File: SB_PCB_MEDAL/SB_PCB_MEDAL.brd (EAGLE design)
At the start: 60 x 60 mm, 41 parts, among them IC1 ATTINY44A-SSU

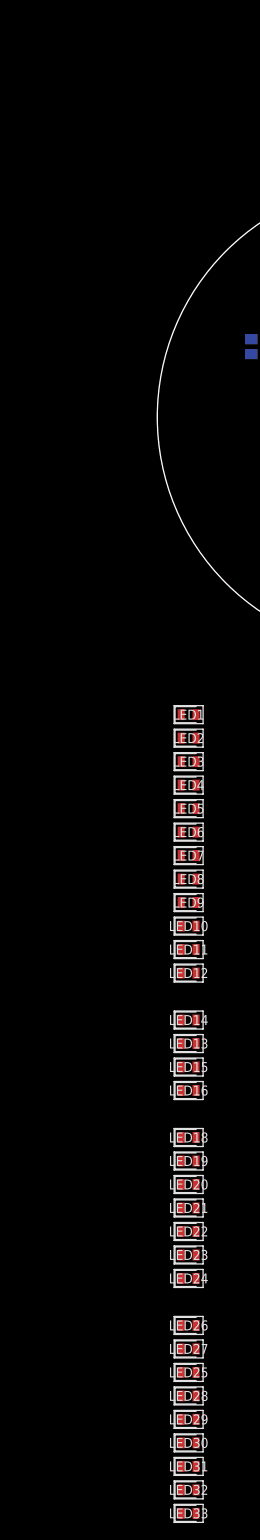
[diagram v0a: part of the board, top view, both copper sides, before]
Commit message: removed 2 additional LEDs
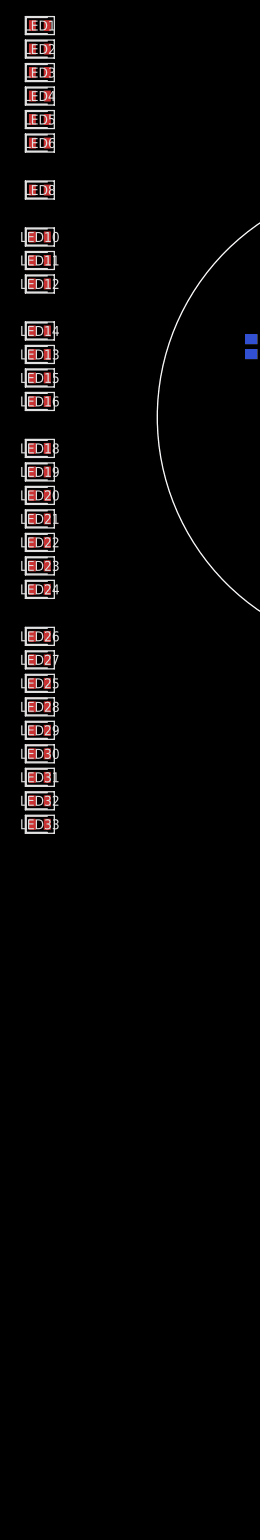
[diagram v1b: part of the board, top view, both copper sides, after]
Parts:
- removed LED7, LED9: KPT-2012CGCK, SamacSys_Parts:LEDC2012X78N
- moved LED1 90.0 mm to (-45.0, 50.0)
- moved LED10 90.0 mm to (-45.0, 23.0)
- moved LED11 90.0 mm to (-45.0, 20.0)
- moved LED12 90.0 mm to (-45.0, 17.0)
- moved LED13 90.0 mm to (-45.0, 8.00)
- moved LED14 90.0 mm to (-45.0, 11.0)
- moved LED15 90.0 mm to (-45.0, 5.00)
- moved LED16 90.0 mm to (-45.0, 2.00)
- moved LED18 90.0 mm to (-45.0, -4.00)
- moved LED19 90.0 mm to (-45.0, -7.00)
- moved LED2 90.0 mm to (-45.0, 47.0)
- moved LED20 90.0 mm to (-45.0, -10.0)
- moved LED21 90.0 mm to (-45.0, -13.0)
- moved LED22 90.0 mm to (-45.0, -16.0)
- moved LED23 90.0 mm to (-45.0, -19.0)
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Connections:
- removed net N$1: LED26.2
- net N$2: no longer LED7.2
- net N$4: no longer LED7.1, LED9.2
- net N$5: no longer LED9.1

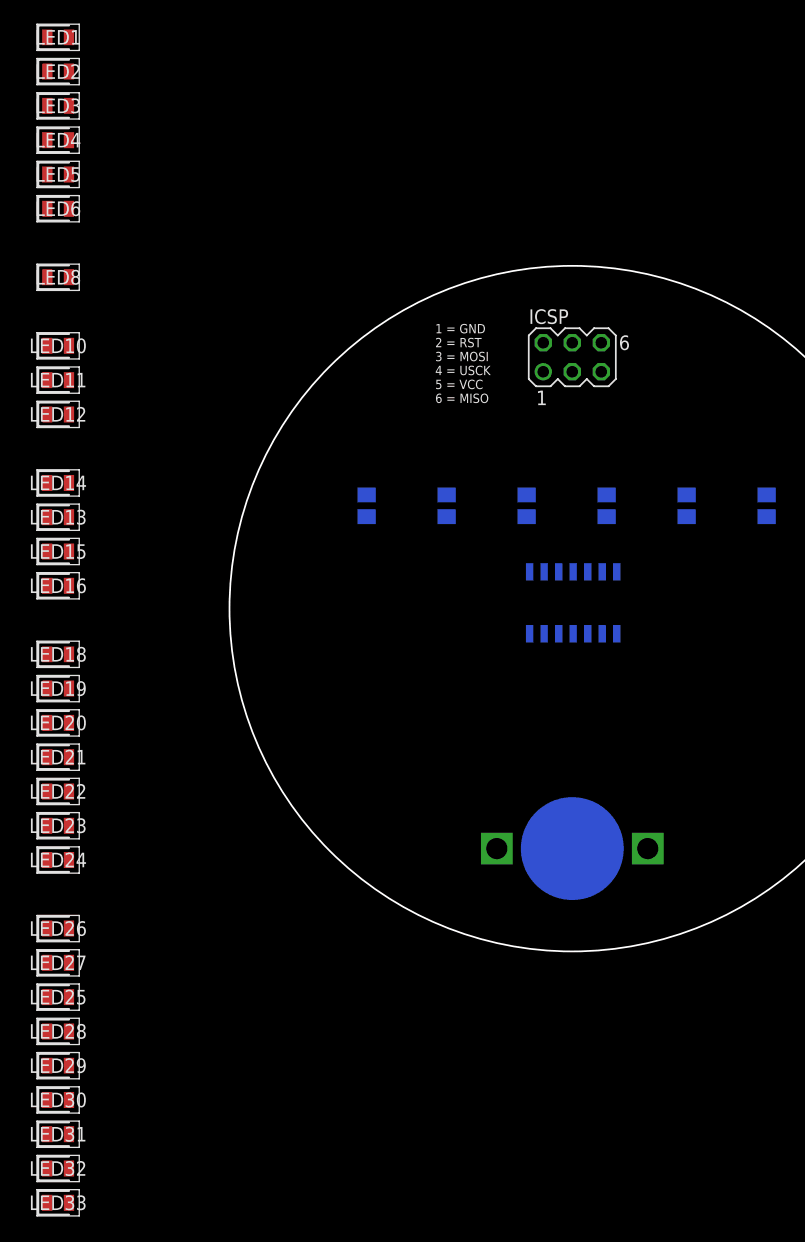
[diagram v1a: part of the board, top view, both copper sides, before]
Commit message: literally copy and paste files from other branch into the master because EAGLE files and branches hate each other as much as North Korea and the US....
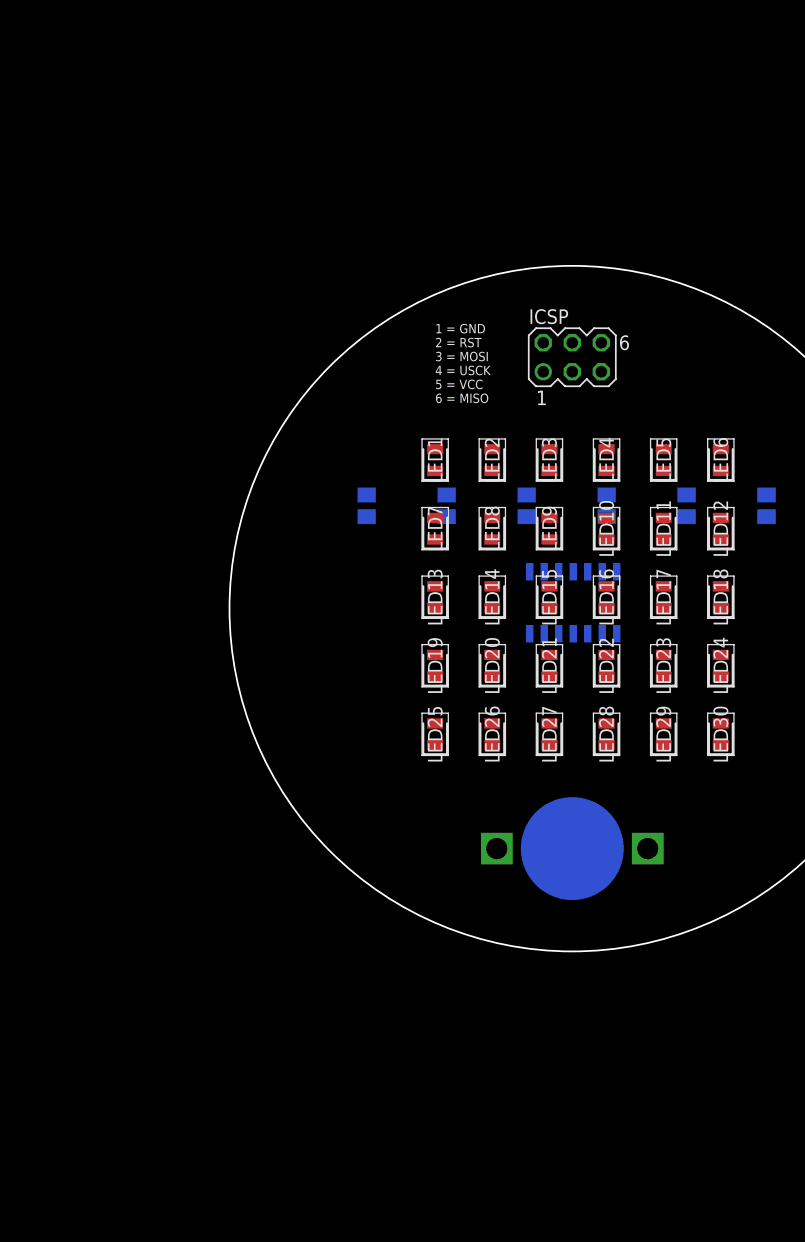
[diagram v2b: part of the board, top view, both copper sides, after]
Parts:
- removed LED31, LED32, LED33: KPT-2012CGCK, SamacSys_Parts:LEDC2012X78N
- added LED17, LED7, LED9: KPT-2012CGCK, SamacSys_Parts:LEDC2012X78N
- moved LED30 66.2 mm to (13.0, -11.0), turned to 90 degrees
- moved LED6 62.0 mm to (13.0, 13.0), turned to 90 degrees
- moved LED24 60.4 mm to (13.0, -5.00), turned to 90 degrees
- moved LED29 60.4 mm to (8.00, -11.0), turned to 90 degrees
- moved LED12 58.9 mm to (13.0, 7.00), turned to 90 degrees
- moved LED5 58.6 mm to (8.00, 13.0), turned to 90 degrees
- moved LED18 58.2 mm to (13.0, 1.00), turned to 90 degrees
- moved LED4 55.6 mm to (3.00, 13.0), turned to 90 degrees
- moved LED23 54.8 mm to (8.00, -5.00), turned to 90 degrees
- moved LED28 54.6 mm to (3.00, -11.0), turned to 90 degrees
- moved LED11 54.6 mm to (8.00, 7.00), turned to 90 degrees
- moved LED3 53.0 mm to (-2.00, 13.0), turned to 90 degrees
- moved LED2 51.0 mm to (-7.00, 13.0), turned to 90 degrees
- moved LED10 50.6 mm to (3.00, 7.00), turned to 90 degrees
- moved LED1 49.6 mm to (-12.0, 13.0), turned to 90 degrees
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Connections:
- removed net N$10: LED2.2, LED4.1
- removed net N$7: LED10.1, LED6.2
- removed net N$8: LED4.2, LED6.1
- new net N$1: LED1.2, LED11.2, LED12.1, LED19.2, LED2.1, LED20.1, LED25.2, LED26.1, LED29.2, LED30.1, R1.2
- new net N$19: IC1.5
- new net N$20: IC1.6
- new net PA0: IC1.13, R1.1
- new net PA1: IC1.12, R2.1
- new net PA2: IC1.11, R3.1
- new net PA3: IC1.10, R4.1
- new net PB0: IC1.2, R5.1
- new net PB1: IC1.3, R6.1
- net N$2: now also LED1.1, LED13.2, LED14.1, LED2.2, LED21.2, LED22.1, LED27.2, LED28.1, LED3.2, LED4.1, R2.2; no longer LED3.1, LED5.2
- net N$3: now also LED11.1, LED12.2, LED15.2, LED16.1, LED23.2, LED24.1, LED3.1, LED4.2, LED5.2, LED6.1, R3.2; no longer LED1.1, LED3.2
- net N$4: now also LED13.1, LED14.2, LED17.2, LED18.1, LED19.1, LED20.2, LED6.2, LED7.2, LED8.1, R4.2; no longer LED8.2
- net N$5: now also LED10.1, LED15.1, LED16.2, LED21.1, LED22.2, LED25.1, LED26.2, LED7.1, LED8.2, LED9.2, R5.2; no longer LED11.2, LED8.1
- net N$6: now also LED17.1, LED18.2, LED23.1, LED24.2, LED27.1, LED28.2, LED29.1, LED30.2, LED9.1, R6.2; no longer LED12.1

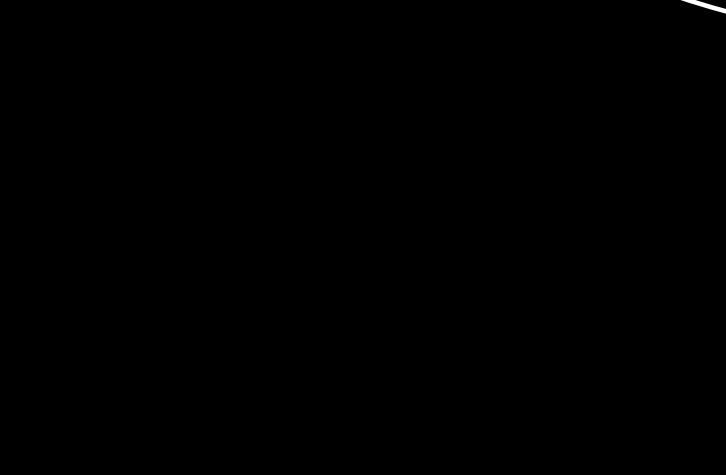
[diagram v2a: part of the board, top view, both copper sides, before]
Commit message: added surface mountable button
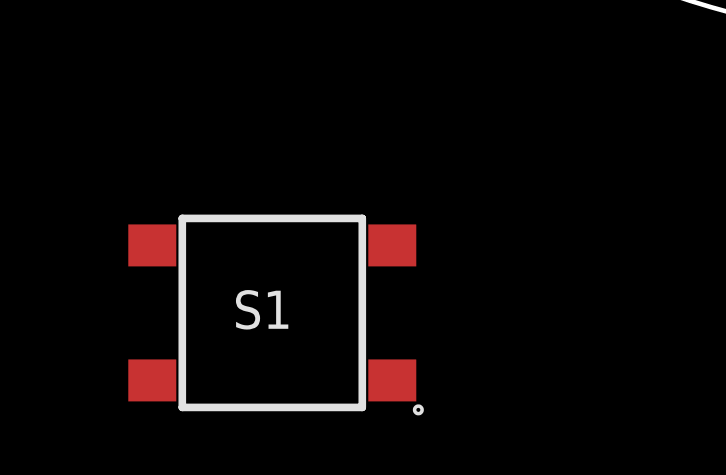
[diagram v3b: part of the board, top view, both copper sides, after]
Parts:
- added S1: B3FS-1000P, SamacSys_Parts:B3FS-1000P
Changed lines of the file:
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@@
 <attribute name="SUPPLIER_NAME" value="RS" x="13" y="-11" size="1.778" layer="27" rot="R90" display="off"/>
+</element>
+<element name="S1" library="SamacSys_Parts" package="B3FS-1000P" value="B3FS-1000P" x="-23" y="-39">
+<attribute name="3D_PACKAGE" value="" x="-23" y="-39" size="1.778" layer="27" display="off"/>
+<attribute name="ALLIED_NUMBER" value="70175891" x="-23" y="-39" size="1.778" layer="27" display="off"/>
+<attribute name="DESCRIPTION" value="Switch Tact,6x6mm,flat act,gen purp,tape Plunger Tactile Switch, SPST-NO 0.05 A@ 24 V dc 0.5mm" x="-23" y="-39" size="1.778" layer="27" display="off"/>
+<attribute name="HEIGHT" value="mm" x="-23" y="-39" size="1.778" layer="27" display="off"/>
+<attribute name="MANUFACTURER_NAME" value="Omron Electronics" x="-23" y="-39" size="1.778" layer="27" display="off"/>
+<attribute name="MANUFACTURER_PART_NUMBER" value="B3FS-1000P" x="-23" y="-39" size="1.778" layer="27" display="off"/>
+<attribute name="OTHER_PART_NUMBER" value="" x="-23" y="-39" size="1.778" layer="27" display="off"/>
+<attribute name="RS_PART_NUMBER" value="6821254P" x="-23" y="-39" size="1.778" layer="27" display="off"/>
+<attribute name="SUPPLIER_NAME" value="RS" x="-23" y="-39" size="1.778" layer="27" display="off"/>
 </element>
 </elements>

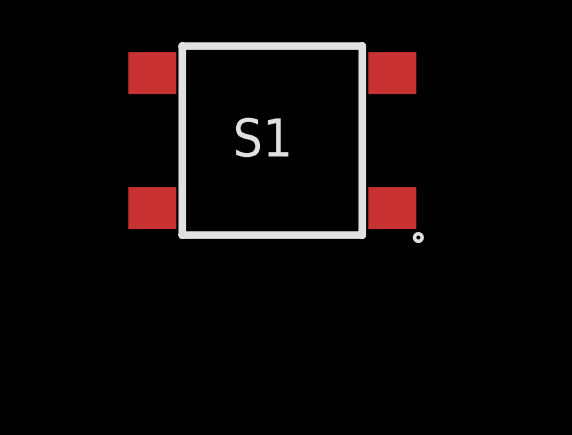
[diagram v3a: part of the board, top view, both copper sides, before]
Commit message: added more labels to the board
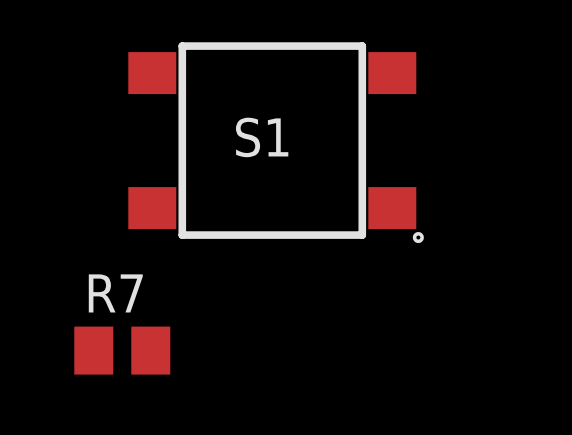
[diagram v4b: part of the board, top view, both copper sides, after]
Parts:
- added R7: 10k Ω, resistor:M0805
- BT1: value (none) -> 3v
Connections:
- removed net N$19: IC1.5
- removed net N$20: IC1.6
- new net N$7: R7.1, S1.4
- new net N$8: S1.3
- net GND: now also IC1.5, IC1.6, S1.1, S1.2
- net VCC: now also R7.2
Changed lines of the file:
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@@
 <attribute name="OC_NEWARK" value="unknown" x="0" y="22" size="1.778" layer="27" display="off"/>
 </element>
-<element name="BT1" library="SparkFun-Batteries" package="BATTCON_12MM_PTH" value="" x="0" y="-21" rot="MR0">
+<element name="BT1" library="SparkFun-Batteries" package="BATTCON_12MM_PTH" value="3v" x="0" y="-21" rot="MR0">
 <attribute name="PROD_ID" value="BATT-08315" x="0" y="-21" size="0.4064" layer="28" rot="MR0" display="off"/>
 <attribute name="SF_SKU" value="PRT-07948" x="0" y="-21" size="0.4064" layer="28" rot="MR0" display="off"/>
@@
 <attribute name="SUPPLIER_NAME" value="RS" x="-23" y="-39" size="1.778" layer="27" display="off"/>
 </element>
+<element name="R7" library="resistor" package="M0805" value="10k Ω" x="-28" y="-46"/>
 </elements>
 <signals>
@@
 <contactref element="ICSP" pad="5"/>
 <contactref element="BT1" pad="VCC@1"/>
+<contactref element="R7" pad="2"/>
+<wire x1="-6.604" y1="-21" x2="-27.05" y2="-46" width="0" layer="19" extent="1-1"/>
 <wire x1="-3.73" y1="3.221" x2="-6.604" y2="-21" width="0" layer="19" extent="16-16"/>
 <wire x1="2.54" y1="20.73" x2="-3.73" y2="3.221" width="0" layer="19" extent="16-16"/>
@@
 <contactref element="IC1" pad="14"/>
 <contactref element="BT1" pad="GND"/>
-<wire x1="-3.73" y1="-2.201" x2="0" y2="-21" width="0" layer="19" extent="1-16"/>
-<wire x1="-2.54" y1="20.73" x2="-3.73" y2="-2.201" width="0" layer="19" extent="16-16"/>
+<contactref element="IC1" pad="5"/>
+<contactref element="IC1" pad="6"/>
+<contactref element="S1" pad="2"/>
+<contactref element="S1" pad="1"/>
+<wire x1="-19" y1="-41.25" x2="-27" y2="-41.25" width="0" layer="19" extent="1-1"/>
+<wire x1="0" y1="-21" x2="-19" y2="-41.25" width="0" layer="19" extent="1-16"/>
+<wire x1="-3.73" y1="-2.201" x2="0" y2="-21" width="0" layer="19" extent="16-16"/>
+<wire x1="1.35" y1="3.221" x2="-3.73" y2="-2.201" width="0" layer="19" extent="16-16"/>
+<wire x1="2.62" y1="3.221" x2="1.35" y2="3.221" width="0" layer="19" extent="16-16"/>
+<wire x1="-2.54" y1="20.73" x2="1.35" y2="3.221" width="0" layer="19" extent="16-16"/>
 </signal>
 <signal name="MISO">
@@
 <wire x1="-1.19" y1="3.221" x2="17" y2="8.05" width="0" layer="19" extent="16-16"/>
 </signal>
-<signal name="N$19">
-<contactref element="IC1" pad="5"/>
-</signal>
-<signal name="N$20">
-<contactref element="IC1" pad="6"/>
+<signal name="N$7">
+<contactref element="S1" pad="4"/>
+<contactref element="R7" pad="1"/>
+<wire x1="-27" y1="-36.75" x2="-28.95" y2="-46" width="0" layer="19" extent="1-1"/>
+</signal>
+<signal name="N$8">
+<contactref element="S1" pad="3"/>
 </signal>
 </signals>

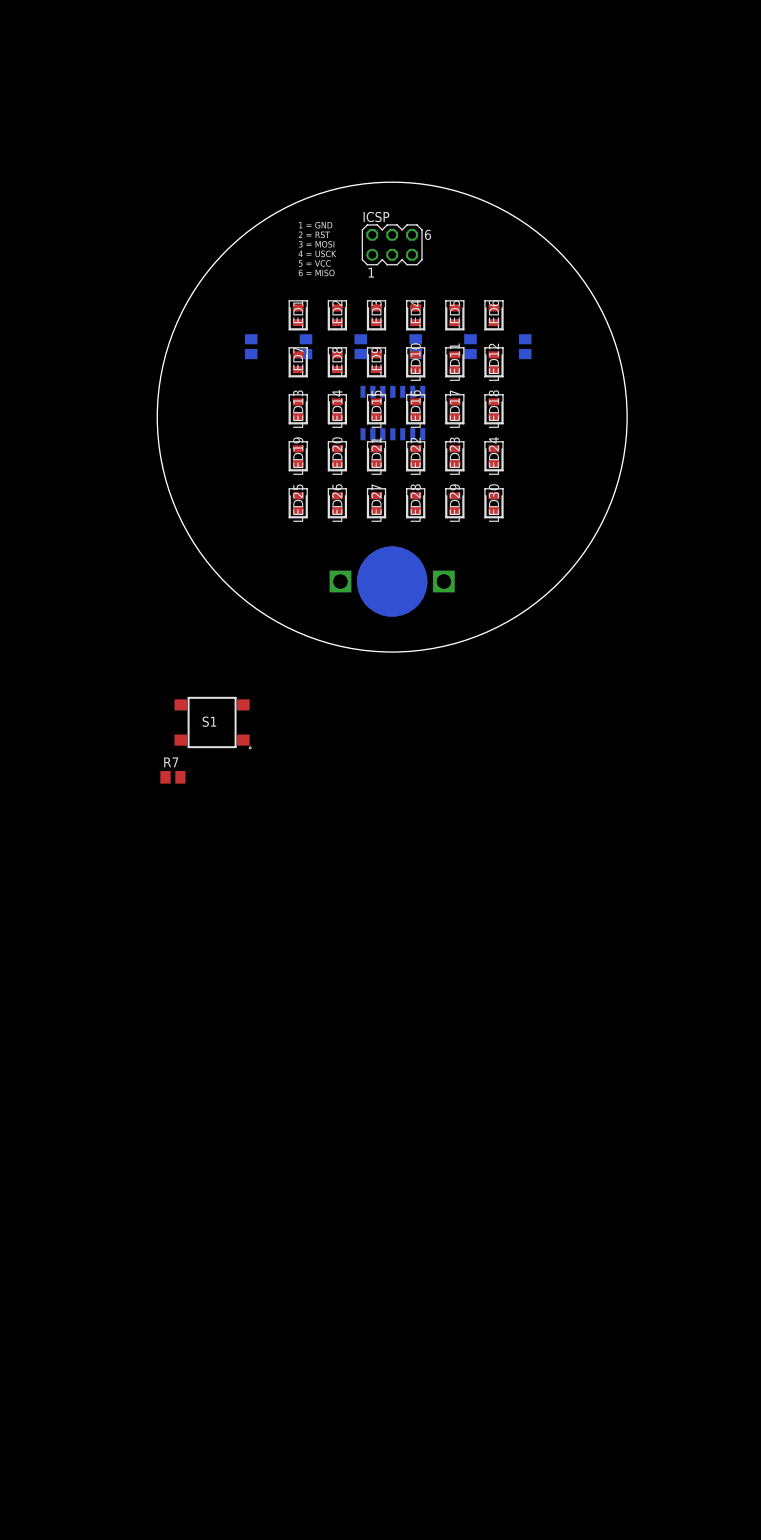
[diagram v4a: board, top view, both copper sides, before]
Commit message: modify led position and add usb
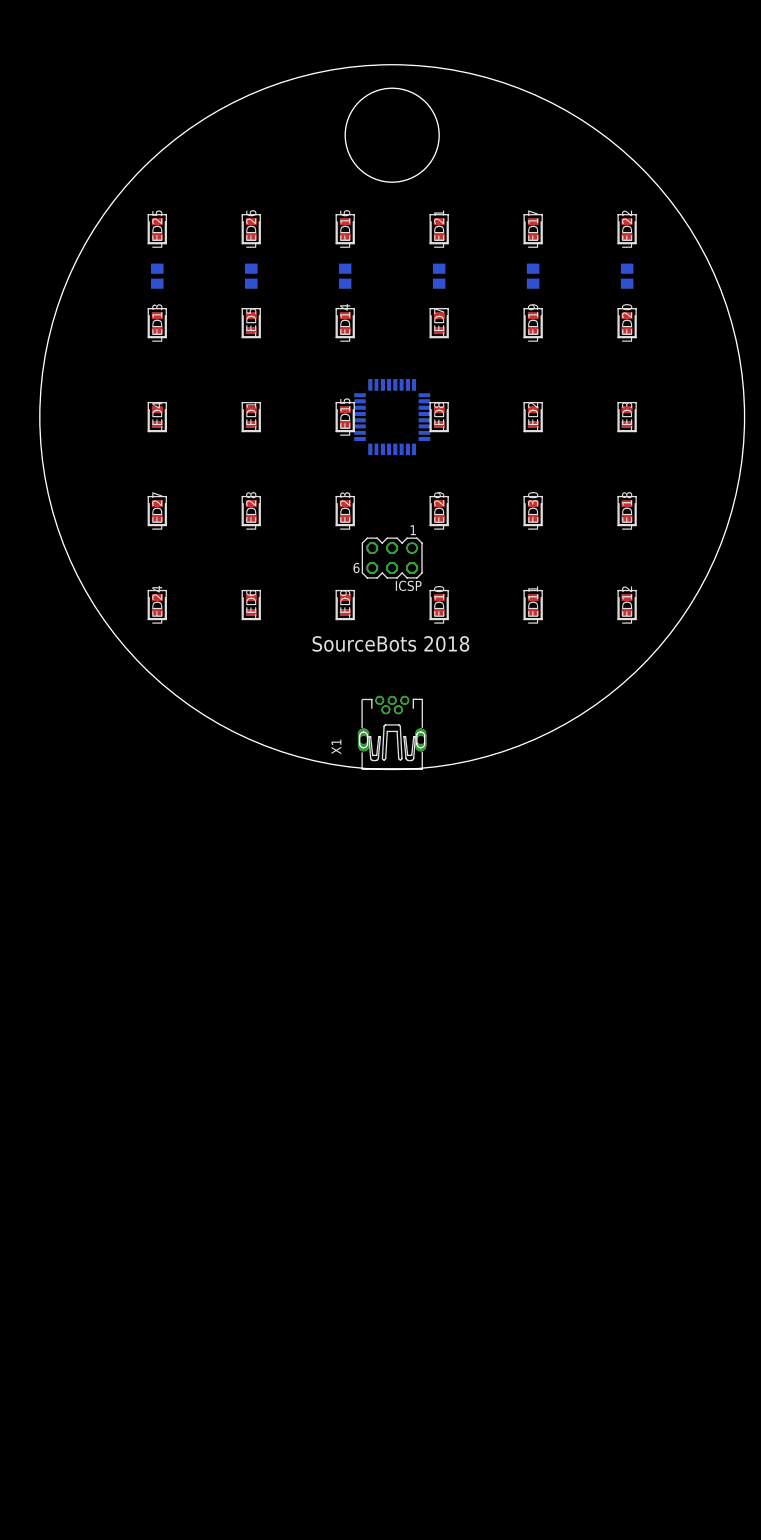
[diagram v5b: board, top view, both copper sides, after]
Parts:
- removed BT1: 3v, SparkFun-Batteries:BATTCON_12MM_PTH
- removed IC1: ATTINY44A-SSU, SamacSys_Parts:SOIC127P600X175-14N
- removed R7: 10k Ω, resistor:M0805
- removed S1: B3FS-1000P, SamacSys_Parts:B3FS-1000P
- added U1: ATMEGA16U2-AU, Atmel_By_element14_Batch_1-00:QFP80P900X900X120-32N
- added X1: MINI-USB_SHIELD5P2-32005-601, con-cypressindustries:32005-601
- moved LED6 48.3 mm to (-18.0, -24.0)
- moved LED24 47.0 mm to (-30.0, -24.0)
- moved LED20 40.7 mm to (30.0, 12.0)
- moved ICSP 40.0 mm to (0.00, -18.0), turned to 180 degrees
- moved LED22 39.6 mm to (30.0, 24.0)
- moved LED25 39.4 mm to (-30.0, 24.0)
- moved LED26 36.7 mm to (-18.0, 24.0)
- moved LED4 35.5 mm to (-30.0, 0.00)
- moved LED12 35.4 mm to (30.0, -24.0)
- moved LED3 34.5 mm to (30.0, 0.00)
- moved LED19 34.5 mm to (18.0, 12.0)
- moved LED11 32.6 mm to (18.0, -24.0)
- moved LED9 31.3 mm to (-6.00, -24.0)
- moved LED10 31.1 mm to (6.00, -24.0)
- moved LED21 30.1 mm to (6.00, 24.0)
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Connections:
- removed net N$7: R7.1, S1.4
- removed net N$8: S1.3
- new net AVCC: U1.32
- new net UVCC: U1.31
- net GND: no longer BT1.GND, IC1.14, IC1.5, IC1.6, S1.1, S1.2
- net MISO: no longer IC1.8
- net MOSI: no longer IC1.7
- net PA0: no longer IC1.13
- net PA1: no longer IC1.12
- net PA2: no longer IC1.11
- net PA3: no longer IC1.10
- net PB0: no longer IC1.2
- net PB1: no longer IC1.3
- net RST: no longer IC1.4
- net USCK: no longer IC1.9
- net VCC: now also U1.4; no longer BT1.VCC@1, IC1.1, R7.2
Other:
- board size 60 x 60 mm -> 90 x 90 mm
